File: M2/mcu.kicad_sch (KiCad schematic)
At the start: 33 parts, among them U2 ESP32-P4NRW16, Y1 32KHz, Y2 40MHz

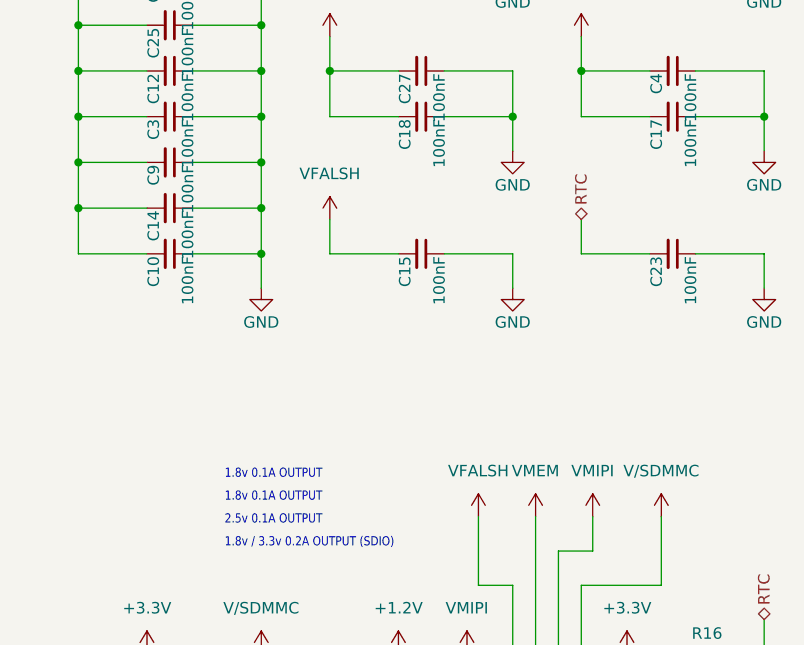
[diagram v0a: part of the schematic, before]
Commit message: Fix typo in schematic for FLASH
Correction on schematic from FALSH to FLASH. Simple typo correction, nothing more.
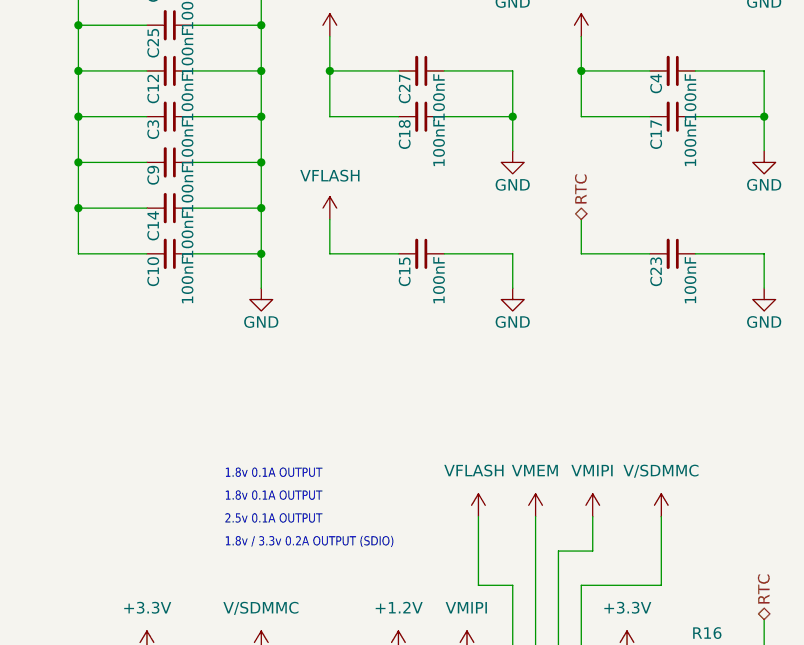
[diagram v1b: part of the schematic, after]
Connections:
- net VFALSH renamed VFLASH
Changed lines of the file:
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@@
 		(on_board yes)
 		(dnp no)
-		(fields_autoplaced yes)
 		(property "Reference" "#PWR039"
 			(at 237.49 109.22 0)
@@
 			)
 		)
-		(property "Value" "VFALSH"
-			(at 237.49 100.33 0)
-			(effects
-				(font
-					(size 1.27 1.27)
-				)
+		(property "Value" "VFLASH"
+			(at 233.68 100.33 0)
+			(effects
+				(font
+					(size 1.27 1.27)
+				)
+				(justify left)
 			)
 		)
@@
 		(on_board yes)
 		(dnp no)
-		(fields_autoplaced yes)
 		(property "Reference" "#PWR036"
 			(at 220.98 76.2 0)
@@
 			)
 		)
-		(property "Value" "VFALSH"
-			(at 220.98 67.31 0)
-			(effects
-				(font
-					(size 1.27 1.27)
-				)
-			)
-		)
+		(property "Value" "VFLASH"
+			(at 217.678 67.564 0)
+			(effects
+				(font
+					(size 1.27 1.27)
+				)
+				(justify left)
+			)
+		)
